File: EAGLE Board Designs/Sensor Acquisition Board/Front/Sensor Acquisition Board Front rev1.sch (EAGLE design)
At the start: 33 parts, among them J1 CONNECTOR-SENSOR_NF_S_RA_BLACK, J10 JUMPER_0603_, J2 CONNECTOR-SENSOR_NF_S_RA_BLACK, J3 CONNECTOR-CAN_NF_S_RA_BLACK, J4 CONNECTOR-CAN_NF_S_RA_BLACK, J6 JUMPER_0603_, U1 VOLTAGE_REGULATOR_SOT-223_5V, U2 MCP2562FD, U3 MCP2562FD

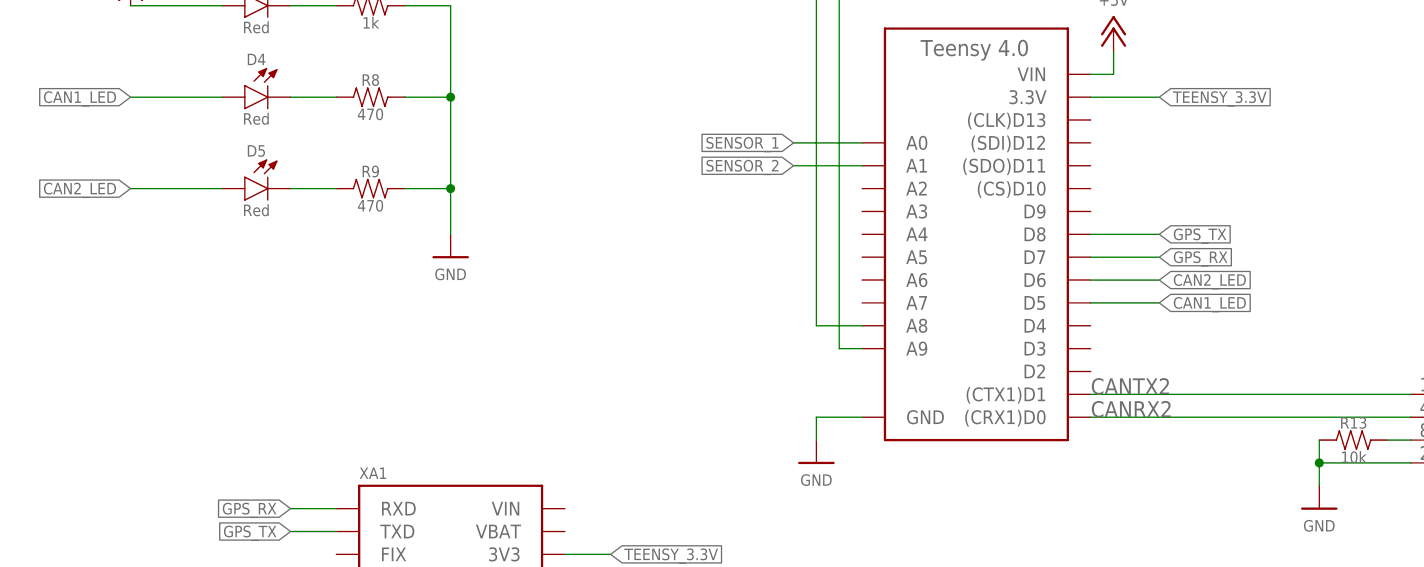
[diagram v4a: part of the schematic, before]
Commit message: Created GPS LED and added GPS to Board
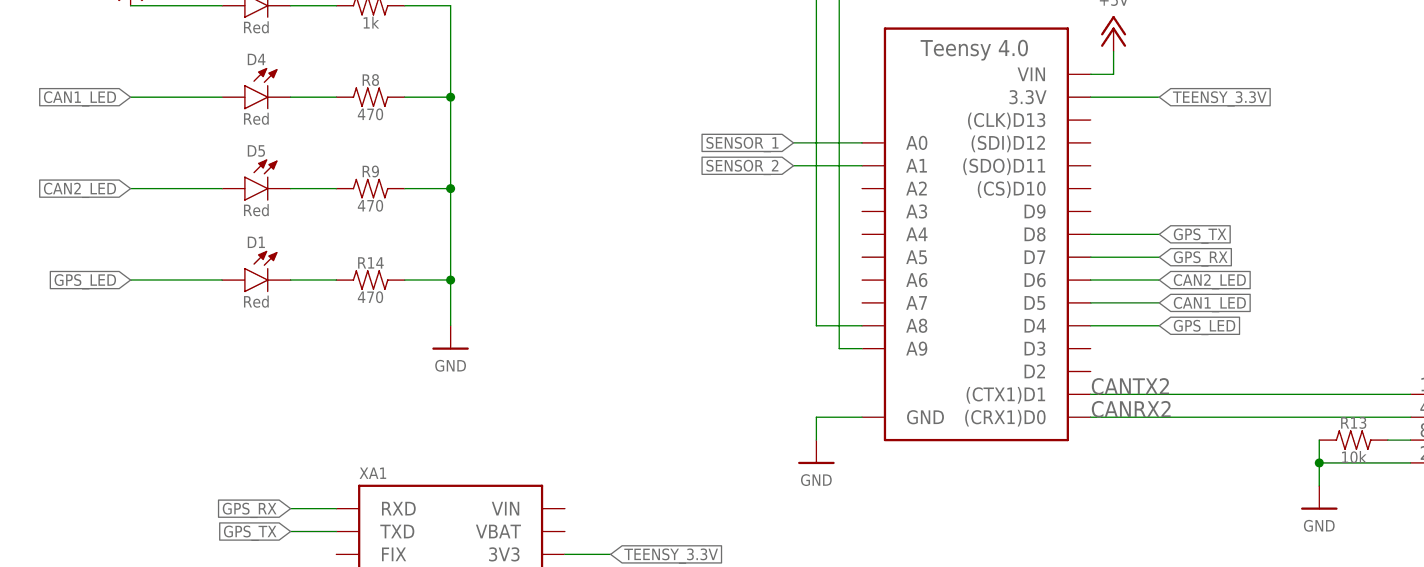
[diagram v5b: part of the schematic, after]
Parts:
- added D1: LED_0603_RED, HyTechDevices:LED_0603_RED
- added R14: RESISTOR_0603_470, HyTechDevices:RESISTOR_0603_470
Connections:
- new net GPS_LED: A2.D4, D1.A
- new net N$4: D1.C, R14.1
- net GND: now also R14.2
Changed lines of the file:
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@@
 <part name="XA1" library="HyTechDevices" deviceset="ULTIMATE_GPS" device=""/>
 <part name="P7" library="HyTechSupplies" deviceset="GND" device=""/>
+<part name="R14" library="HyTechDevices" deviceset="RESISTOR_?_*" device="0603" technology="470" value="RESISTOR_0603_470"/>
+<part name="D1" library="HyTechDevices" deviceset="LED_?_*" device="0603" technology="RED"/>
 </parts>
 <sheets>
@@
 <attribute name="NAME" x="46.99" y="107.696" size="1.27" layer="96" align="bottom-center"/>
 </instance>
-<instance part="P20" gate="1" x="68.58" y="96.52" smashed="yes">
-<attribute name="VALUE" x="68.58" y="95.25" size="1.27" layer="96" align="top-center"/>
+<instance part="P20" gate="1" x="68.58" y="86.36" smashed="yes">
+<attribute name="VALUE" x="68.58" y="85.09" size="1.27" layer="96" align="top-center"/>
 </instance>
 <instance part="P21" gate="1" x="33.02" y="127" smashed="yes">
@@
 <instance part="P7" gate="1" x="53.34" y="53.34" smashed="yes">
 <attribute name="VALUE" x="53.34" y="52.07" size="1.27" layer="96" align="top-center"/>
+</instance>
+<instance part="R14" gate="G$1" x="60.96" y="93.98" smashed="yes">
+<attribute name="NAME" x="59.69" y="95.25" size="1.27" layer="95" align="bottom-center"/>
+<attribute name="RESISTANCE" x="59.69" y="92.71" size="1.27" layer="96" align="top-center"/>
+</instance>
+<instance part="D1" gate="LED" x="48.26" y="93.98" smashed="yes">
+<attribute name="COLOR" x="46.99" y="92.202" size="1.27" layer="95" align="top-center"/>
+<attribute name="NAME" x="46.99" y="97.536" size="1.27" layer="96" align="bottom-center"/>
 </instance>
 </instances>
@@
 <pinref part="R8" gate="G$1" pin="2"/>
 <wire x1="68.58" y1="114.3" x2="68.58" y2="104.14" width="0.1524" layer="91"/>
-<wire x1="68.58" y1="104.14" x2="68.58" y2="99.06" width="0.1524" layer="91"/>
+<wire x1="68.58" y1="104.14" x2="68.58" y2="93.98" width="0.1524" layer="91"/>
+<wire x1="68.58" y1="93.98" x2="68.58" y2="88.9" width="0.1524" layer="91"/>
 <wire x1="63.5" y1="114.3" x2="68.58" y2="114.3" width="0.1524" layer="91"/>
 <junction x="68.58" y="114.3"/>
@@
 <junction x="68.58" y="104.14"/>
 <pinref part="P20" gate="1" pin="GND"/>
+<pinref part="R14" gate="G$1" pin="2"/>
+<wire x1="63.5" y1="93.98" x2="68.58" y2="93.98" width="0.1524" layer="91"/>
+<junction x="68.58" y="93.98"/>
 </segment>
 <segment>
@@
 </segment>
 </net>
+<net name="GPS_LED" class="0">
+<segment>
+<pinref part="A2" gate="G$1" pin="D4"/>
+<wire x1="139.7" y1="88.9" x2="147.32" y2="88.9" width="0.1524" layer="91"/>
+<label x="147.32" y="88.9" size="1.27" layer="95" xref="yes"/>
+</segment>
+<segment>
+<pinref part="D1" gate="LED" pin="A"/>
+<wire x1="43.18" y1="93.98" x2="33.02" y2="93.98" width="0.1524" layer="91"/>
+<label x="33.02" y="93.98" size="1.27" layer="95" rot="MR0" xref="yes"/>
+</segment>
+</net>
+<net name="N$4" class="0">
+<segment>
+<pinref part="D1" gate="LED" pin="C"/>
+<pinref part="R14" gate="G$1" pin="1"/>
+<wire x1="50.8" y1="93.98" x2="55.88" y2="93.98" width="0.1524" layer="91"/>
+</segment>
+</net>

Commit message: Fixed front
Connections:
- net GPS_LED: now also XA1.FIX; no longer A2.D4
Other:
- note added: "Translates 2 Analog Voltage Sensors to CAN and Supplies GPS Information"
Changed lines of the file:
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@@
 <sheet>
 <plain>
+<text x="197.104" y="10.922" size="2.54" layer="95">Translates 2 Analog Voltage Sensors to CAN and
+ Supplies GPS Information</text>
 </plain>
 <instances>
@@
 <attribute name="ENGINEER" x="129.54" y="22.86" size="2.54" layer="95"/>
 <attribute name="DESIGNER_FURTHER" x="176.53" y="30.48" size="2.54" layer="95"/>
-<attribute name="DESCRIPTION_1" x="196.85" y="15.24" size="2.54" layer="95"/>
 <attribute name="DESCRIPTION_2" x="176.53" y="10.16" size="2.54" layer="95"/>
 <attribute name="REVIEWER_BOARD" x="227.33" y="38.1" size="2.54" layer="95"/>
@@
 </segment>
 </net>
-<net name="GPS_LED" class="0">
-<segment>
-<pinref part="A2" gate="G$1" pin="D4"/>
-<wire x1="139.7" y1="88.9" x2="147.32" y2="88.9" width="0.1524" layer="91"/>
-<label x="147.32" y="88.9" size="1.27" layer="95" xref="yes"/>
-</segment>
-<segment>
-<pinref part="D1" gate="LED" pin="A"/>
-<wire x1="43.18" y1="93.98" x2="33.02" y2="93.98" width="0.1524" layer="91"/>
-<label x="33.02" y="93.98" size="1.27" layer="95" rot="MR0" xref="yes"/>
-</segment>
-</net>
 <net name="N$4" class="0">
 <segment>
@@
 </segment>
 </net>
+<net name="GPS_LED" class="0">
+<segment>
+<pinref part="D1" gate="LED" pin="A"/>
+<wire x1="43.18" y1="93.98" x2="33.02" y2="93.98" width="0.1524" layer="91"/>
+<label x="33.02" y="93.98" size="1.27" layer="95" rot="R180" xref="yes"/>
+</segment>
+<segment>
+<label x="50.8" y="63.5" size="1.27" layer="95" rot="R180" xref="yes"/>
+<pinref part="XA1" gate="G$1" pin="FIX"/>
+<wire x1="50.8" y1="63.5" x2="55.88" y2="63.5" width="0.1524" layer="91"/>
+</segment>
+</net>

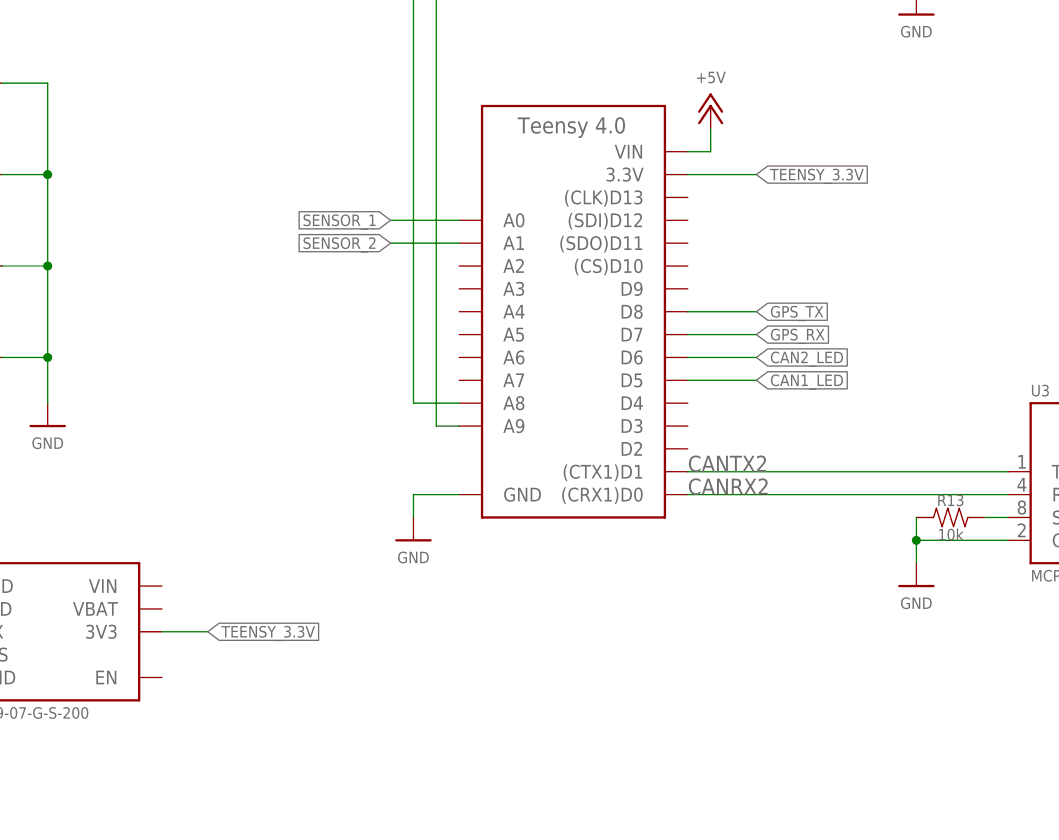
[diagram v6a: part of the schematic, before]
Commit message: Fixed GPS connections
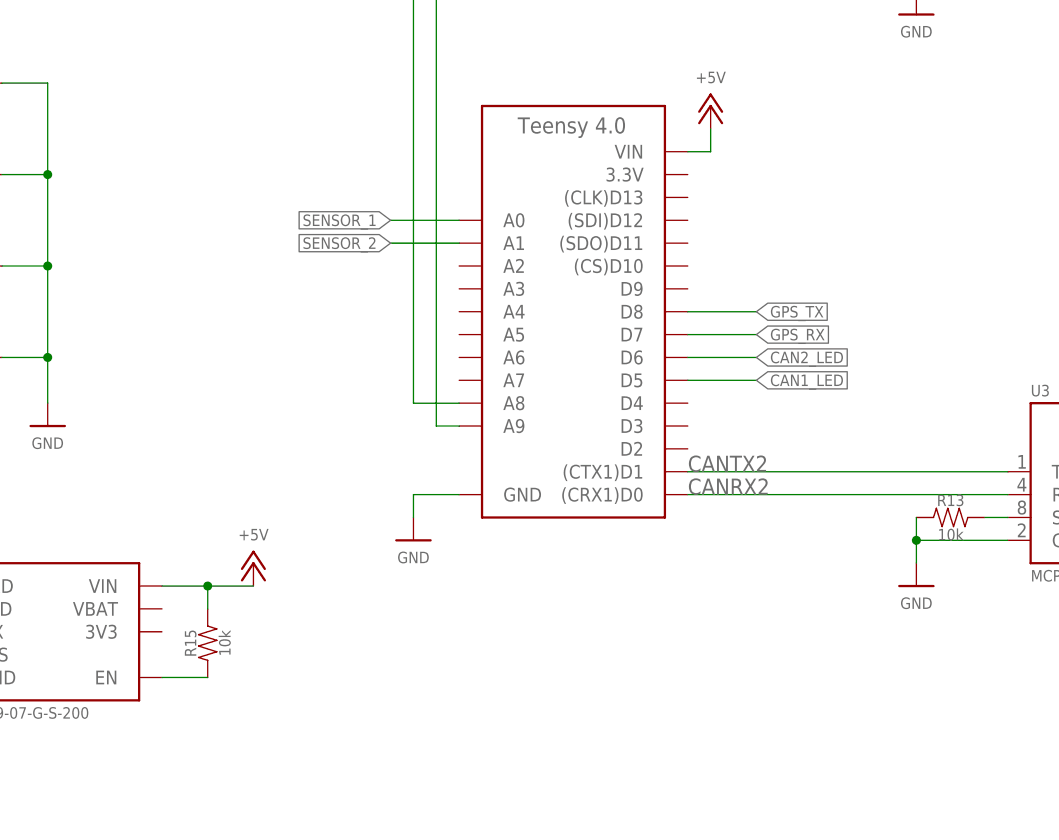
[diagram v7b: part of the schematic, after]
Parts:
- added R15: RESISTOR_0603_10K, HyTechDevices:RESISTOR_0603_10K
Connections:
- new net N$7: R15.1, XA1.EN
- net +5V: now also R15.2, XA1.VIN
- net TEENSY_3.3V: no longer A2.3.3V, XA1.3V3
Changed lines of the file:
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@@
 <part name="R14" library="HyTechDevices" deviceset="RESISTOR_?_*" device="0603" technology="470" value="RESISTOR_0603_470"/>
 <part name="D1" library="HyTechDevices" deviceset="LED_?_*" device="0603" technology="RED"/>
+<part name="R15" library="HyTechDevices" deviceset="RESISTOR_?_*" device="0603" technology="10K"/>
+<part name="P9" library="HyTechSupplies" deviceset="+5V" device=""/>
 </parts>
 <sheets>
@@
 <attribute name="NAME" x="46.99" y="97.536" size="1.27" layer="96" align="bottom-center"/>
 </instance>
+<instance part="R15" gate="G$1" x="86.36" y="63.5" smashed="yes" rot="R90">
+<attribute name="NAME" x="85.09" y="62.23" size="1.27" layer="95" rot="R90" align="bottom-center"/>
+<attribute name="RESISTANCE" x="87.63" y="62.23" size="1.27" layer="96" rot="R90" align="top-center"/>
+</instance>
+<instance part="P9" gate="1" x="91.44" y="71.12" smashed="yes">
+<attribute name="VALUE" x="91.44" y="73.66" size="1.27" layer="96" align="bottom-center"/>
+</instance>
 </instances>
 <busses>
@@
 <pinref part="P21" gate="1" pin="+5V"/>
 </segment>
+<segment>
+<pinref part="XA1" gate="G$1" pin="VIN"/>
+<wire x1="81.28" y1="68.58" x2="86.36" y2="68.58" width="0.1524" layer="91"/>
+<pinref part="R15" gate="G$1" pin="2"/>
+<wire x1="86.36" y1="66.04" x2="86.36" y2="68.58" width="0.1524" layer="91"/>
+<pinref part="P9" gate="1" pin="+5V"/>
+<wire x1="86.36" y1="68.58" x2="91.44" y2="68.58" width="0.1524" layer="91"/>
+<junction x="86.36" y="68.58"/>
+</segment>
 </net>
 <net name="+12V" class="0">
@@
 <net name="TEENSY_3.3V" class="0">
 <segment>
-<wire x1="139.7" y1="114.3" x2="147.32" y2="114.3" width="0.1524" layer="91"/>
-<label x="147.32" y="114.3" size="1.27" layer="95" xref="yes"/>
-<pinref part="A2" gate="G$1" pin="3.3V"/>
-</segment>
-<segment>
 <label x="200.66" y="83.82" size="1.27" layer="95" xref="yes"/>
 <pinref part="U3" gate="G$1" pin="VIO"/>
@@
 <pinref part="U2" gate="G$1" pin="VIO"/>
 <wire x1="198.12" y1="149.86" x2="200.66" y2="149.86" width="0.1524" layer="91"/>
-</segment>
-<segment>
-<pinref part="XA1" gate="G$1" pin="3V3"/>
-<wire x1="81.28" y1="63.5" x2="86.36" y2="63.5" width="0.1524" layer="91"/>
-<label x="86.36" y="63.5" size="1.27" layer="95" xref="yes"/>
 </segment>
 </net>
@@
 </segment>
 </net>
+<net name="N$7" class="0">
+<segment>
+<pinref part="XA1" gate="G$1" pin="EN"/>
+<wire x1="81.28" y1="58.42" x2="86.36" y2="58.42" width="0.1524" layer="91"/>
+<pinref part="R15" gate="G$1" pin="1"/>
+</segment>
+</net>
